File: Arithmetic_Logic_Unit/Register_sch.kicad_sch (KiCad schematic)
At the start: 22 parts, among them U1 74LS245, U16 74LS173, U3 74LS173

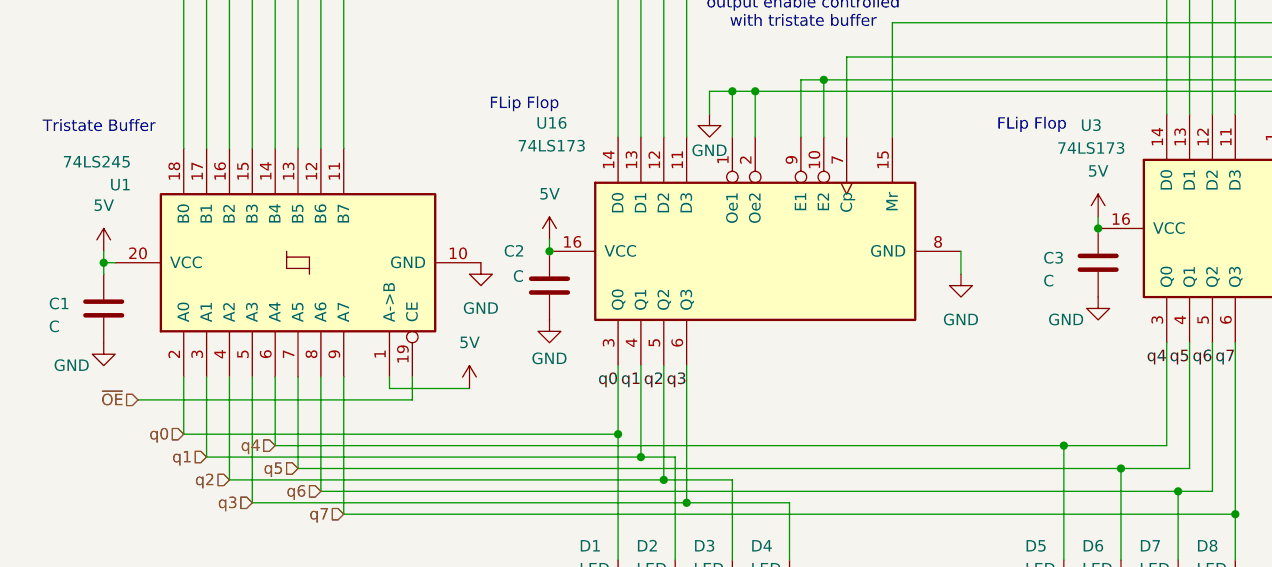
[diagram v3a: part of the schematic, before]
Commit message: preliminary board layout, will move IR to clock module
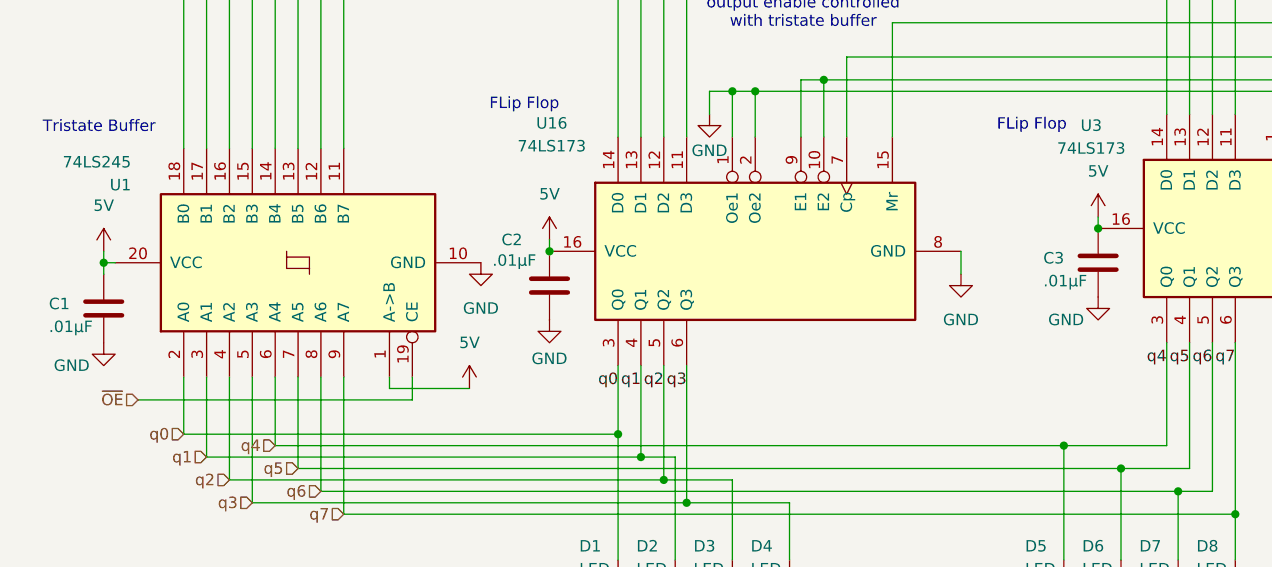
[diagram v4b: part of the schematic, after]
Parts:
- C1, C2, C3: value C -> .01µF; footprint (none) -> Capacitor_THT:C_Disc_D5.0mm_W2.5mm_P2.50mm
- D1, D2, D3, D4, D5, D6, D7, D8: footprint (none) -> LED_THT:LED_D5.0mm
- R1, R2, R3, R4, R5, R6, R7, R8: footprint (none) -> Resistor_THT:R_Axial_DIN0207_L6.3mm_D2.5mm_P5.08mm_Vertical
- U1: footprint (none) -> Package_DIP:DIP-20_W7.62mm
- U16, U3: footprint (none) -> Package_DIP:DIP-16_W7.62mm
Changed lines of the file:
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@@
 			)
 		)
-		(property "Footprint" ""
+		(property "Footprint" "Package_DIP:DIP-20_W7.62mm"
 			(at 57.15 60.96 0)
 			(effects
@@
 			)
 		)
-		(property "Footprint" ""
+		(property "Footprint" "LED_THT:LED_D5.0mm"
 			(at 148.59 97.79 0)
 			(effects
@@
 			)
 		)
-		(property "Footprint" ""
+		(property "Footprint" "LED_THT:LED_D5.0mm"
 			(at 99.06 97.79 0)
 			(effects
@@
 			)
 		)
-		(property "Footprint" ""
+		(property "Footprint" "LED_THT:LED_D5.0mm"
 			(at 142.24 97.79 0)
 			(effects
@@
 			)
 		)
-		(property "Footprint" ""
+		(property "Footprint" "LED_THT:LED_D5.0mm"
 			(at 105.41 97.79 0)
 			(effects
@@
 			)
 		)
-		(property "Footprint" ""
+		(property "Footprint" "Resistor_THT:R_Axial_DIN0207_L6.3mm_D2.5mm_P5.08mm_Vertical"
 			(at 146.812 111.76 90)
 			(effects
@@
 			)
 		)
-		(property "Footprint" ""
+		(property "Footprint" "Resistor_THT:R_Axial_DIN0207_L6.3mm_D2.5mm_P5.08mm_Vertical"
 			(at 109.982 111.76 90)
 			(effects
@@
 			)
 		)
-		(property "Footprint" ""
+		(property "Footprint" "Resistor_THT:R_Axial_DIN0207_L6.3mm_D2.5mm_P5.08mm_Vertical"
 			(at 159.512 111.76 90)
 			(effects
@@
 			)
 		)
-		(property "Value" "C"
+		(property "Value" ".01µF"
 			(at 29.464 68.072 0)
 			(effects
@@
 			)
 		)
-		(property "Footprint" ""
+		(property "Footprint" "Capacitor_THT:C_Disc_D5.0mm_W2.5mm_P2.50mm"
 			(at 34.5948 62.23 0)
 			(effects
@@
 			)
 		)
-		(property "Footprint" ""
+		(property "Footprint" "Resistor_THT:R_Axial_DIN0207_L6.3mm_D2.5mm_P5.08mm_Vertical"
 			(at 103.632 111.76 90)
 			(effects
@@
 		(dnp no)
 		(property "Reference" "C2"
-			(at 80.01 59.69 0)
+			(at 79.756 58.42 0)
 			(effects
 				(font
@@
 			)
 		)
-		(property "Value" "C"
-			(at 81.026 62.484 0)
+		(property "Value" ".01µF"
+			(at 78.74 60.706 0)
 			(effects
 				(font
@@
 			)
 		)
-		(property "Footprint" ""
+		(property "Footprint" "Capacitor_THT:C_Disc_D5.0mm_W2.5mm_P2.50mm"
 			(at 84.1248 59.69 0)
 			(effects
@@
 			)
 		)
-		(property "Footprint" ""
+		(property "Footprint" "LED_THT:LED_D5.0mm"
 			(at 154.94 97.79 0)
 			(effects
@@
 			)
 		)
-		(property "Footprint" ""
+		(property "Footprint" "Package_DIP:DIP-16_W7.62mm"
 			(at 168.91 57.15 0)
 			(effects
@@
 			)
 		)
-		(property "Value" "C"
+		(property "Value" ".01µF"
 			(at 139.954 62.992 0)
 			(effects
@@
 			)
 		)
-		(property "Footprint" ""
+		(property "Footprint" "Capacitor_THT:C_Disc_D5.0mm_W2.5mm_P2.50mm"
 			(at 145.0848 57.15 0)
 			(effects
@@
 			)
 		)
-		(property "Footprint" ""
+		(property "Footprint" "LED_THT:LED_D5.0mm"
 			(at 111.76 97.79 0)
 			(effects
@@
 			)
 		)
-		(property "Footprint" ""
+		(property "Footprint" "Resistor_THT:R_Axial_DIN0207_L6.3mm_D2.5mm_P5.08mm_Vertical"
 			(at 90.932 111.76 90)
 			(effects
@@
 			)
 		)
-		(property "Footprint" ""
+		(property "Footprint" "LED_THT:LED_D5.0mm"
 			(at 92.71 97.79 0)
 			(effects
@@
 			)
 		)
-		(property "Footprint" ""
+		(property "Footprint" "Package_DIP:DIP-16_W7.62mm"
 			(at 107.95 59.69 0)
 			(effects
@@
 			)
 		)
-		(property "Footprint" ""
+		(property "Footprint" "Resistor_THT:R_Axial_DIN0207_L6.3mm_D2.5mm_P5.08mm_Vertical"
 			(at 153.162 111.76 90)
 			(effects
@@
 			)
 		)
-		(property "Footprint" ""
+		(property "Footprint" "LED_THT:LED_D5.0mm"
 			(at 161.29 97.79 0)
 			(effects
@@
 			)
 		)
-		(property "Footprint" ""
+		(property "Footprint" "Resistor_THT:R_Axial_DIN0207_L6.3mm_D2.5mm_P5.08mm_Vertical"
 			(at 97.282 111.76 90)
 			(effects
@@
 			)
 		)
-		(property "Footprint" ""
+		(property "Footprint" "Resistor_THT:R_Axial_DIN0207_L6.3mm_D2.5mm_P5.08mm_Vertical"
 			(at 140.462 111.76 90)
 			(effects

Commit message: layed out PCB
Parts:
- renumbered C1 to C12, C2 to C13, C3 to C14, D1 to D17, D2 to D18, D3 to D19, D4 to D20, D5 to D21, D6 to D22, D7 to D23, D8 to D24, R1 to R17, R2 to R18, R3 to R19, R4 to R20, R5 to R21, R6 to R22, R7 to R23, R8 to R24, U1 to U12, U16 to U13, U3 to U14

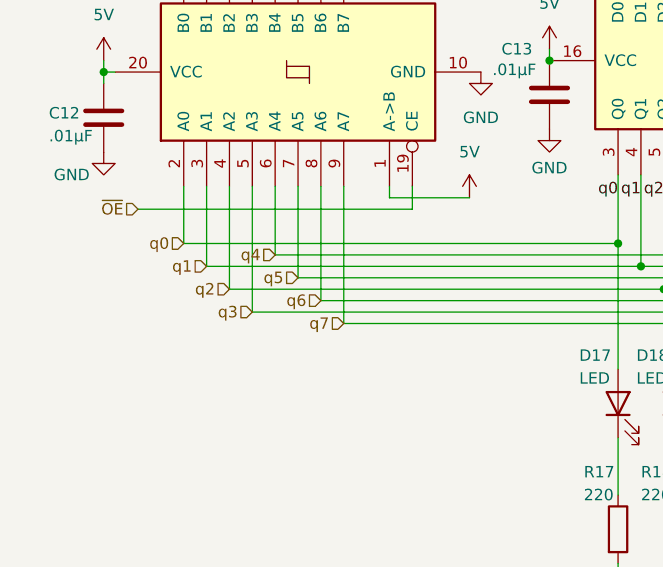
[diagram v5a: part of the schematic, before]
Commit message: Placed clock module again
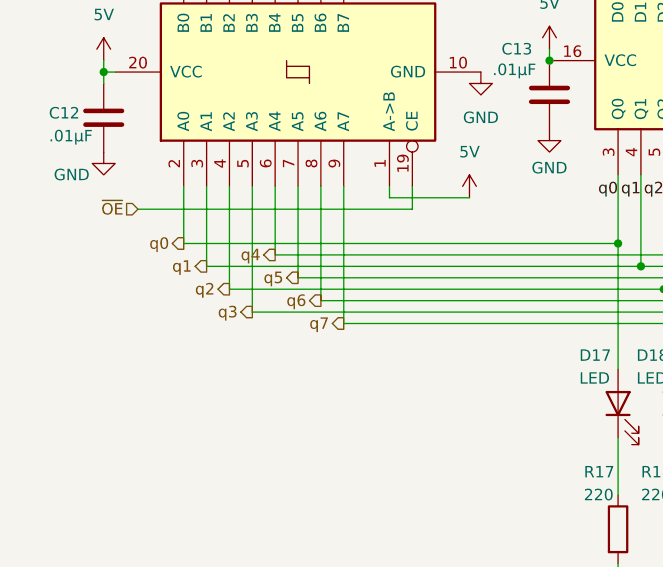
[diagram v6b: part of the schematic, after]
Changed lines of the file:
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@@
 	)
 	(hierarchical_label "q1"
-		(shape input)
+		(shape output)
 		(at 46.99 82.55 180)
 		(fields_autoplaced yes)
@@
 	)
 	(hierarchical_label "q7"
-		(shape input)
+		(shape output)
 		(at 62.23 88.9 180)
 		(fields_autoplaced yes)
@@
 	)
 	(hierarchical_label "q6"
-		(shape input)
+		(shape output)
 		(at 59.69 86.36 180)
 		(fields_autoplaced yes)
@@
 	)
 	(hierarchical_label "q2"
-		(shape input)
+		(shape output)
 		(at 49.53 85.09 180)
 		(fields_autoplaced yes)
@@
 	)
 	(hierarchical_label "q0"
-		(shape input)
+		(shape output)
 		(at 44.45 80.01 180)
 		(fields_autoplaced yes)
@@
 	)
 	(hierarchical_label "q5"
-		(shape input)
+		(shape output)
 		(at 57.15 83.82 180)
 		(fields_autoplaced yes)
@@
 	)
 	(hierarchical_label "q4"
-		(shape input)
+		(shape output)
 		(at 54.61 81.28 180)
 		(fields_autoplaced yes)
@@
 	)
 	(hierarchical_label "q3"
-		(shape input)
+		(shape output)
 		(at 52.07 87.63 180)
 		(fields_autoplaced yes)

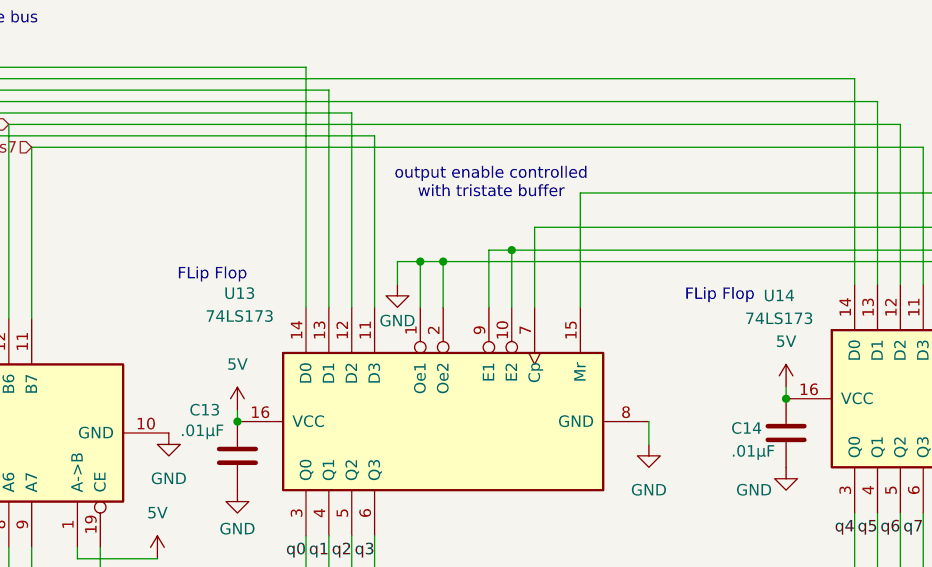
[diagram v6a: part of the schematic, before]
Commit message: returning to pc104 standard
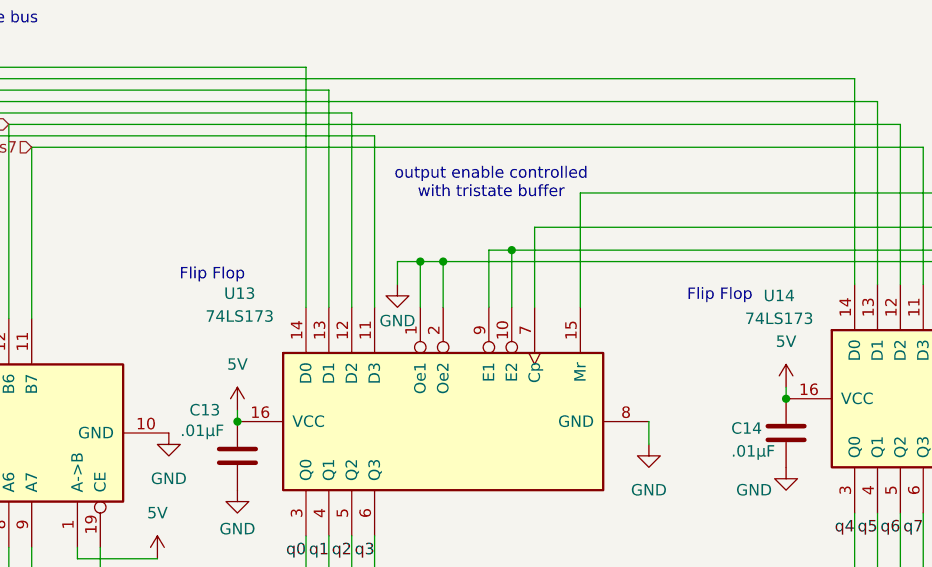
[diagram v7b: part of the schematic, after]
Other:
- note added: "Flip Flop"
- note removed: "FLip Flop"
